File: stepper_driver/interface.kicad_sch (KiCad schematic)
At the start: 15 parts, among them J1 Conn_FFC_20_Pin, J2 Conn_TERM_HDR_01x08_Pin_3.5MM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, U2 MAX6817, U3 LTC2854CDD, U4 SN65LVDM050QDRQ1, U7 LVDS_4-4_HALF_DS91M040TSQE

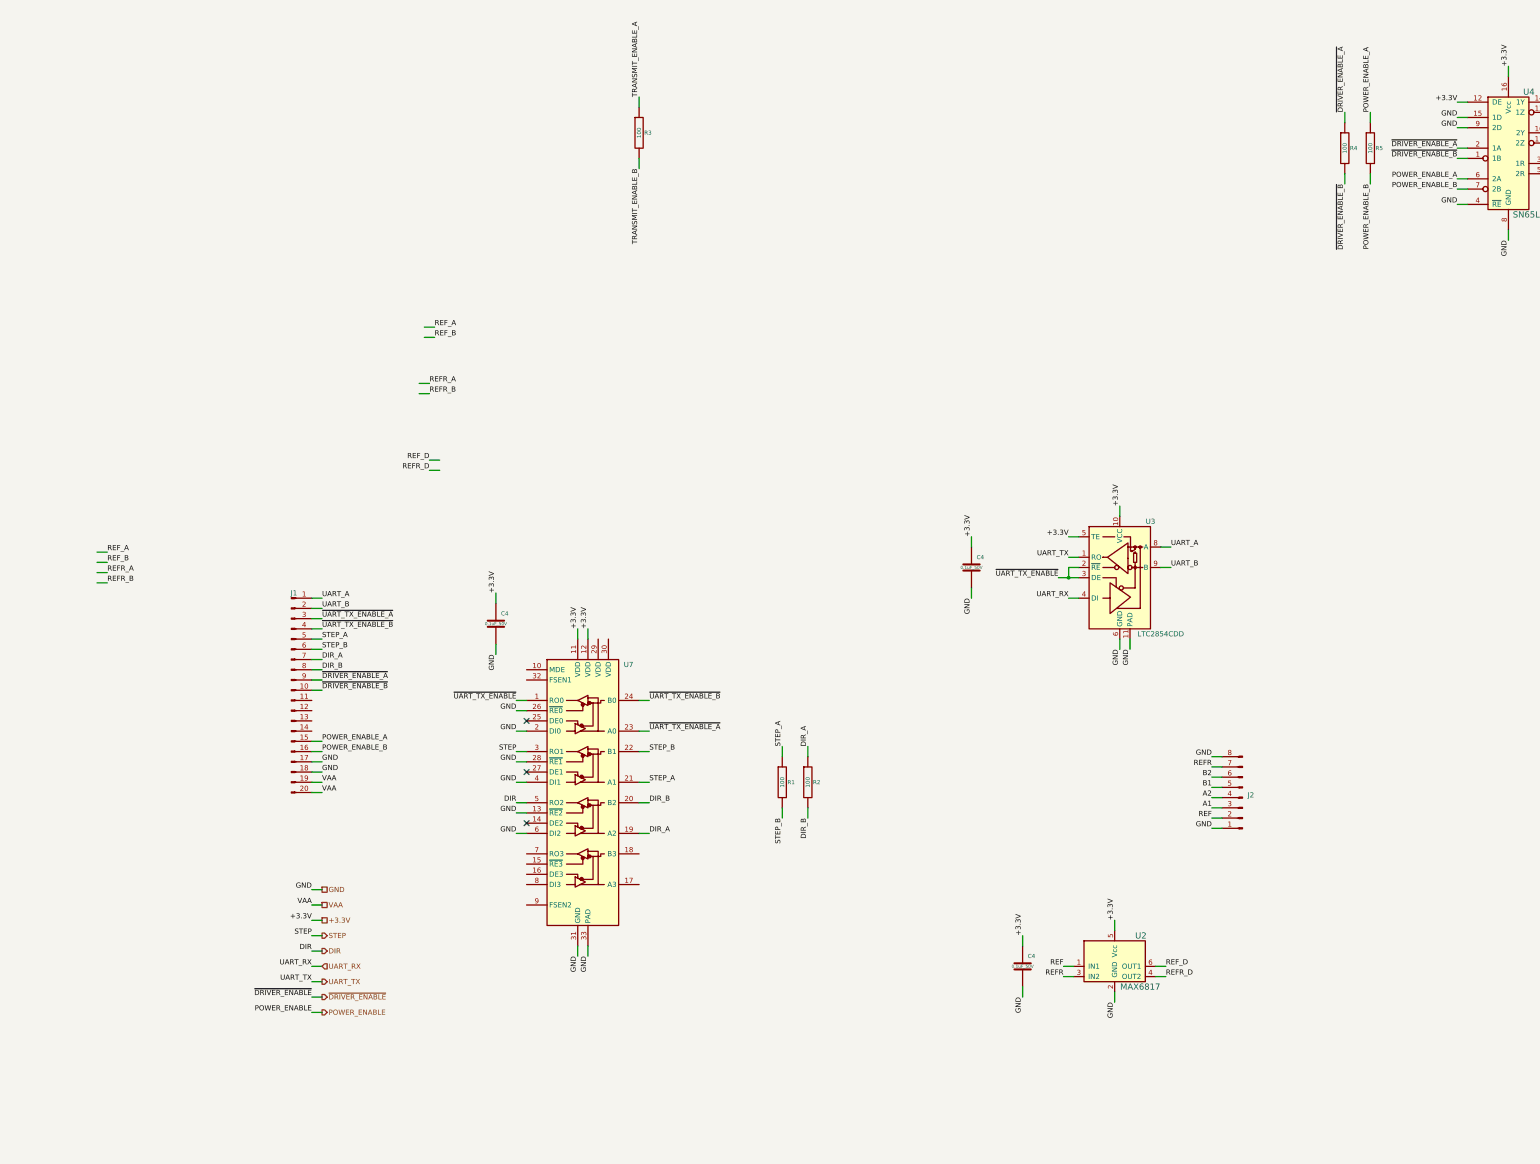
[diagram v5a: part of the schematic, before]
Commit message: Add datasheets
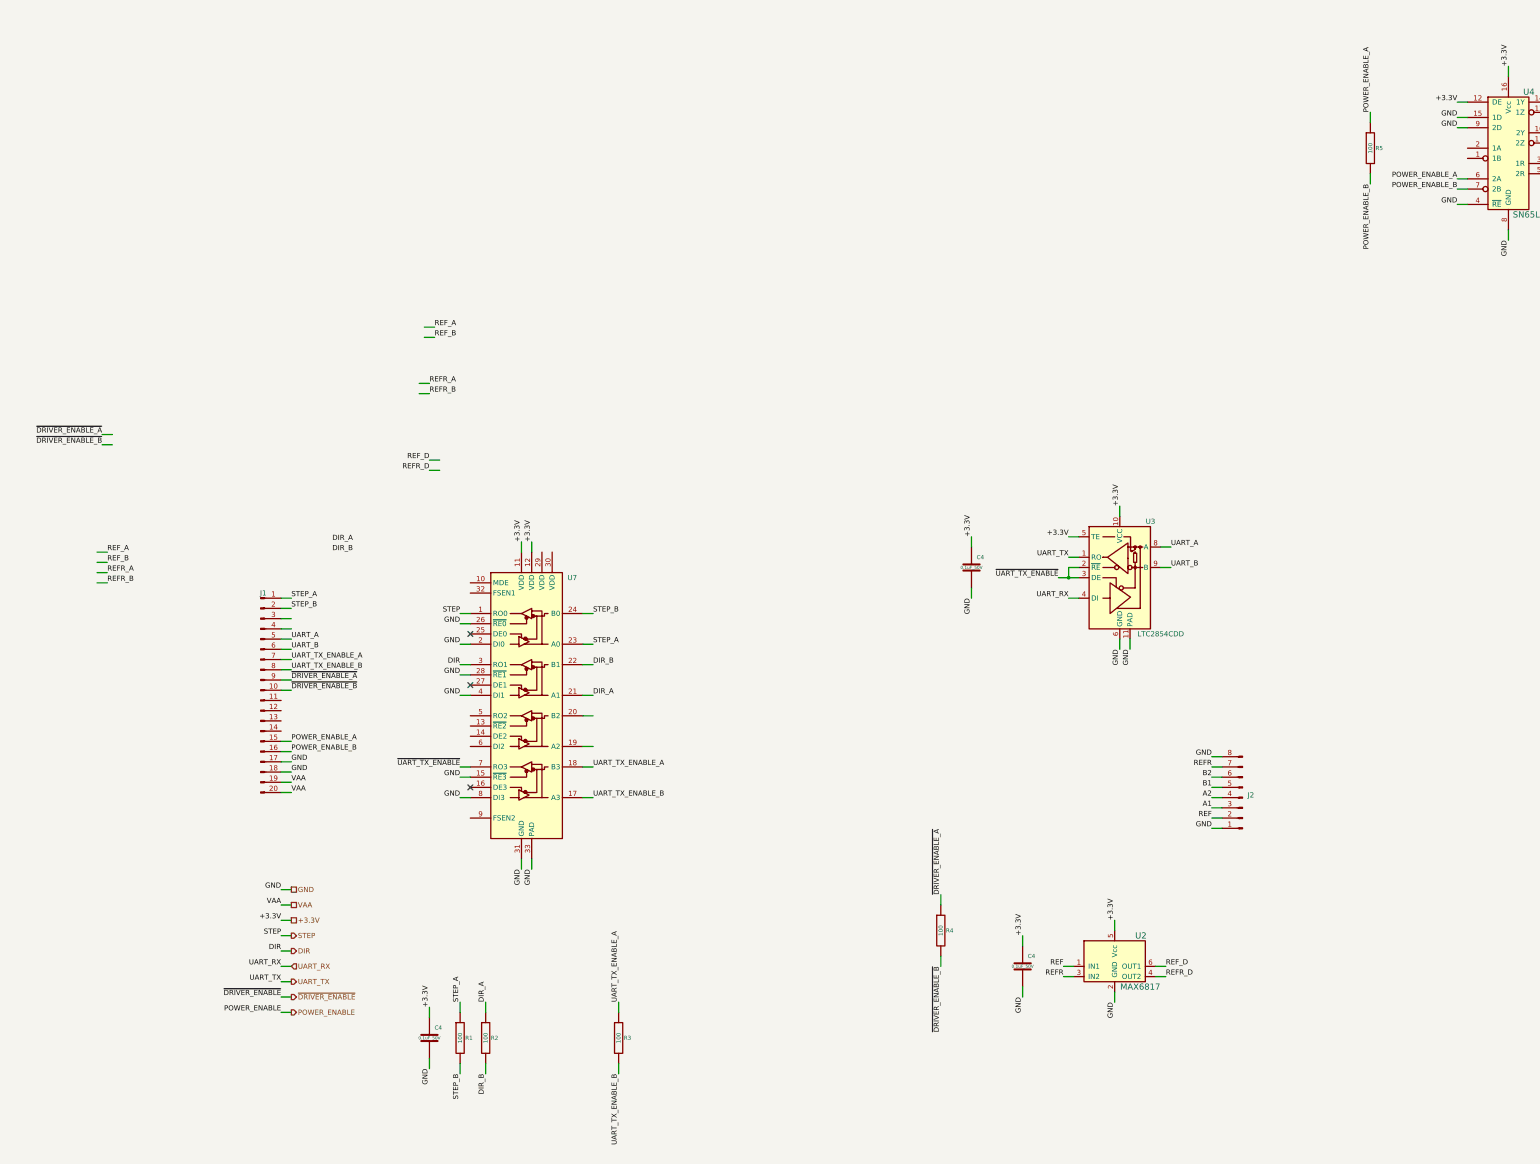
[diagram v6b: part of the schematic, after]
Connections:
- net TRANSMIT_ENABLE_A is gone; now on net UART_TX_ENABLE_A: R3.1
- net TRANSMIT_ENABLE_B is gone; now on net UART_TX_ENABLE_B: R3.2
- net DIR: now also U7.3 (RO1); no longer U7.5 (RO2)
- net DIR_A: now also U7.21 (A1); no longer J1.7 (Pin_7), U7.19 (A2)
- net DIR_B: now also U7.22 (B1); no longer J1.8 (Pin_8), U7.20 (B2)
- net GND: now also U7.15 (~{RE3}), U7.8 (DI3); no longer U7.13 (~{RE2}), U7.6 (DI2)
- net STEP: now also U7.1 (RO0); no longer U7.3 (RO1)
- net STEP_A: now also J1.1 (Pin_1), U7.23 (A0); no longer J1.5 (Pin_5), U7.21 (A1)
- net STEP_B: now also J1.2 (Pin_2), U7.24 (B0); no longer J1.6 (Pin_6), U7.22 (B1)
- net UART_A: now also J1.5 (Pin_5); no longer J1.1 (Pin_1)
- net UART_B: now also J1.6 (Pin_6); no longer J1.2 (Pin_2)
- net ~{DRIVER_ENABLE_A}: no longer U4.2 (1A)
- net ~{DRIVER_ENABLE_B}: no longer U4.1 (1B)
- net ~{UART_TX_ENABLE}: now also U7.7 (RO3); no longer U7.1 (RO0)
- net UART_TX_ENABLE_B: now reaches U7.17 (A3)
- net UART_TX_ENABLE_B: now also J1.8 (Pin_8)
- net UART_TX_ENABLE_A: now reaches U7.18 (B3)
- net UART_TX_ENABLE_A: now also J1.7 (Pin_7)
- net ~{UART_TX_ENABLE_A}: no longer names the net of J1.3 (Pin_3)
- net ~{UART_TX_ENABLE_A}: no longer U7.23 (A0)
- net ~{UART_TX_ENABLE_B}: no longer names the net of J1.4 (Pin_4)
- net ~{UART_TX_ENABLE_B}: no longer U7.24 (B0)
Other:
- moved on the sheet: C4, J1, R1, R2, R3, R4, U7

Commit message: Increase connector pitch from 0.5mm to 1mm
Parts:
- removed C4 (x2): 0.1uF_50V, Janelia:C_0603_1608Metric, symbol Janelia:C_0.1uF_50V_0603
- removed J1: Conn_FFC_20_Pin, Janelia:FFC_Samtec_ZF5S-20-01-T-WT_1x20-1MP_P0.50mm_Horizontal, symbol Janelia:Conn_FFC_20_Pin_ZF5S-20-01-T-WT
- removed U3: LTC2854CDD, Janelia:DFN-10_DD_LIT-L, symbol Janelia:LTC2854CDD
- removed U4: SN65LVDM050QDRQ1, Janelia:D16-L, symbol Janelia:SN65LVDM050QDRQ1
- added C4: 0.1uF_50V, Janelia:C_0603_1608Metric, symbol Janelia:C_0.1uF_50V_0603
- added J1: Conn_FFC_20_Pin_1mm_bottom-ZF1-20-01-T-WT-TR, Janelia:FFC_Samtec_ZF1-20-01-X-WT-Xx20-1MP_P1mm_Horizontal, symbol Janelia:Conn_FFC_20_Pin_1mm_bottom-ZF1-20-01-T-WT-TR
- added R4, R6, R7: 100, Janelia:R_0402_1005Metric, symbol Janelia:R_100_0402
- added U2: LVDS_4-4_HALF_DS91M040TSQE, Janelia:DS91M040TSQE_NOPB, symbol Janelia:LVDS_4-4_HALF_DS91M040TSQE
- renumbered R4 to R5, R5 to R8, U7 to U1
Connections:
- net +3.3V: now also U1.29 (VDD), U1.30 (VDD), C4.1, U2.11 (VDD), U2.12 (VDD), U2.14 (DE2), U2.27 (DE1), U2.29 (VDD), U2.30 (VDD)
- net DIR_A: now also J1.3 (Pin_3)
- net DIR_B: now also J1.4 (Pin_4)
- net GND: now also U1.13 (~{RE2}), U1.6 (DI2), C4.2, J1.17 (Pin_17), J1.18 (Pin_18), U2.15 (~{RE3}), U2.2 (DI0), U2.26 (~{RE0}), U2.31 (GND), U2.33 (PAD), U2.8 (DI3); no longer U1.15 (~{RE3}), U1.8 (DI3)
- net POWER_ENABLE: now also U2.7 (RO3)
- net POWER_ENABLE_A: now also J1.15 (Pin_15), U2.17 (A3)
- net POWER_ENABLE_B: now also J1.16 (Pin_16), U2.18 (B3)
- net REFR_A: now also J1.13 (Pin_13), R7.1, U2.19 (A2)
- net REFR_B: now also J1.14 (Pin_14), R7.2, U2.20 (B2)
- net REFR_D: now also U2.6 (DI2)
- net REF_A: now also J1.11 (Pin_11), R6.1, U2.21 (A1)
- net REF_B: now also J1.12 (Pin_12), R6.2, U2.22 (B1)
- net REF_D: now also U2.4 (DI1)
- net STEP_A: now also J1.1 (Pin_1)
- net STEP_B: now also J1.2 (Pin_2)
- net UART_A: now also U1.17 (A3), J1.7 (Pin_7), R4.1
- net UART_B: now also U1.18 (B3), J1.8 (Pin_8), R4.2
- net UART_RX: now also U1.8 (DI3)
- net UART_TX: now also U1.7 (RO3)
- net VAA: now also J1.19 (Pin_19), J1.20 (Pin_20)
- net ~{DRIVER_ENABLE_A}: now also J1.9 (Pin_9), U2.23 (A0)
- net ~{DRIVER_ENABLE_B}: now also J1.10 (Pin_10), U2.24 (B0)
- net ~{DRIVER_ENABLE}: now also U2.1 (RO0)
- net ~{UART_TX_ENABLE}: now also U1.15 (~{RE3}), U1.16 (DE3), U1.5 (RO2); no longer U1.7 (RO3)
- net ~{UART_TX_ENABLE_A}: now reaches U1.19 (A2)
- net ~{UART_TX_ENABLE_A}: now also R3.1, J1.5 (Pin_5)
- net ~{UART_TX_ENABLE_B}: now reaches U1.20 (B2)
- net ~{UART_TX_ENABLE_B}: now also R3.2, J1.6 (Pin_6)
- removed net UART_TX_ENABLE_A: R3.1, U1.18 (B3)
- removed net UART_TX_ENABLE_B: R3.2, U1.17 (A3)
- no-connect marks 7 -> 9
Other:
- moved on the sheet: C4, J2, R1, R2, R3, R5, R8, U1, U2
